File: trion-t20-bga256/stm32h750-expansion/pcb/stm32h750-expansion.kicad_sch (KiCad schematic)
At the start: 77 parts, among them J1 CONN_02x18, J2 CORTEX_DEBUG_ETM, J3 U.FL, J4 U.FL, J5 U.FL, J6 CONN_01X03, J7 CONN_01X03, J8 PMOD_HOST, M1 MECHANICAL, U1 STM32H750XBH6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

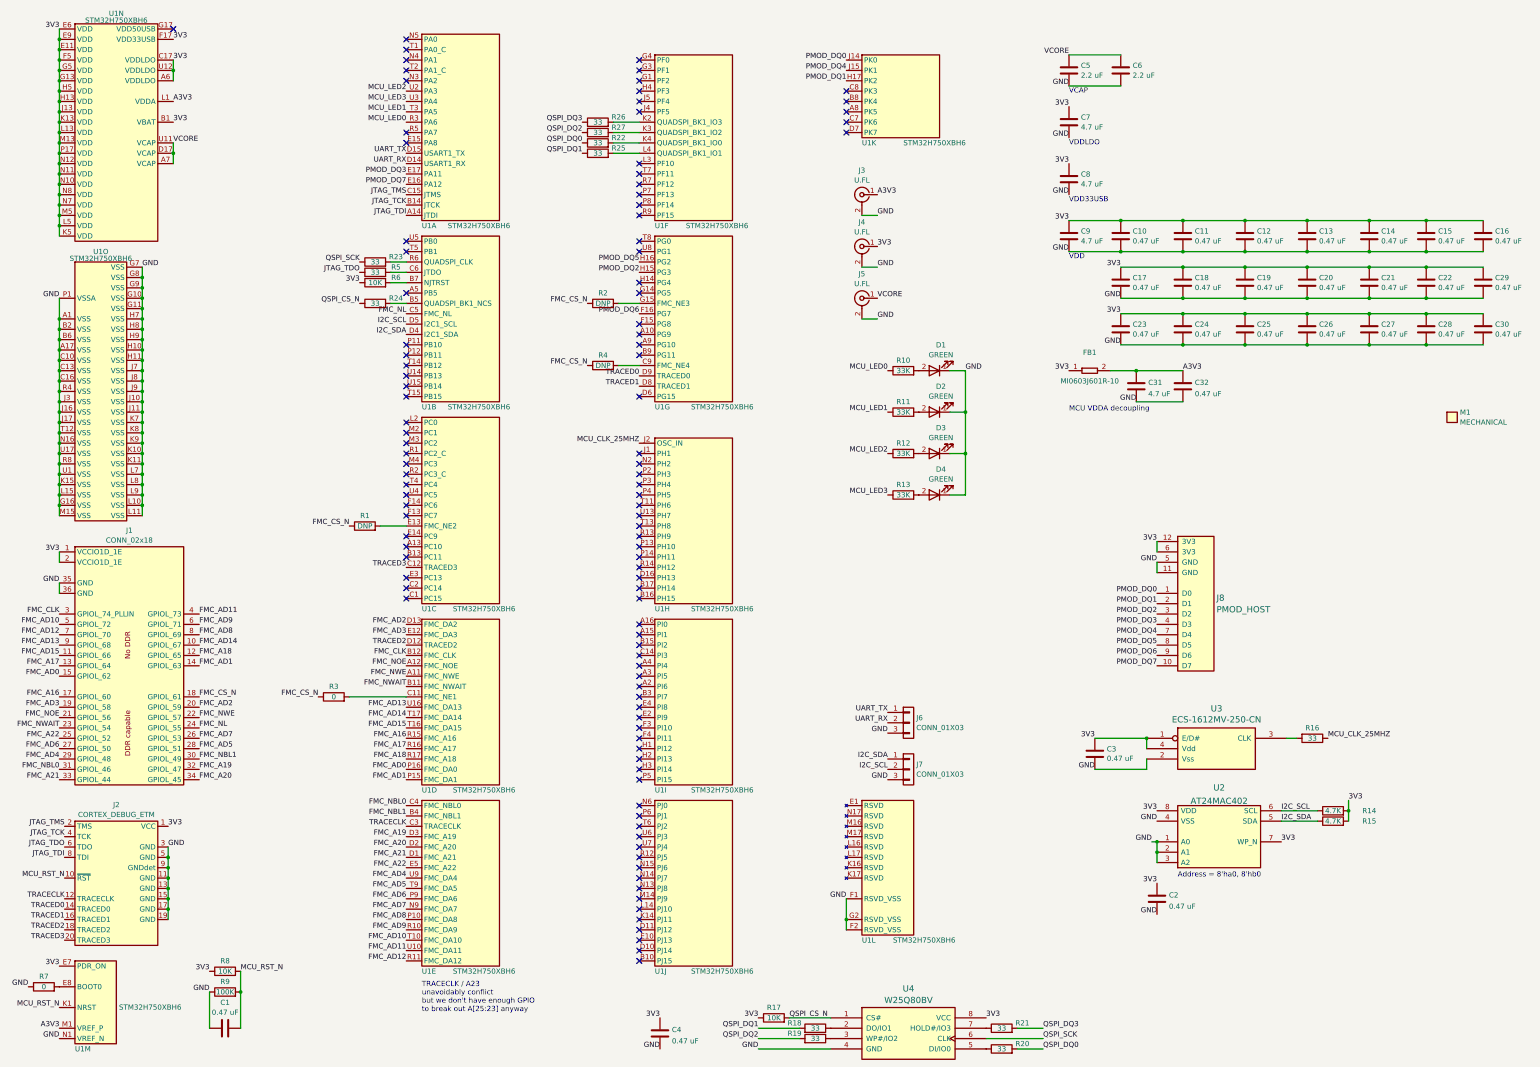
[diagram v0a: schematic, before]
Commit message: Updated stm32h750-expansion for v0.2
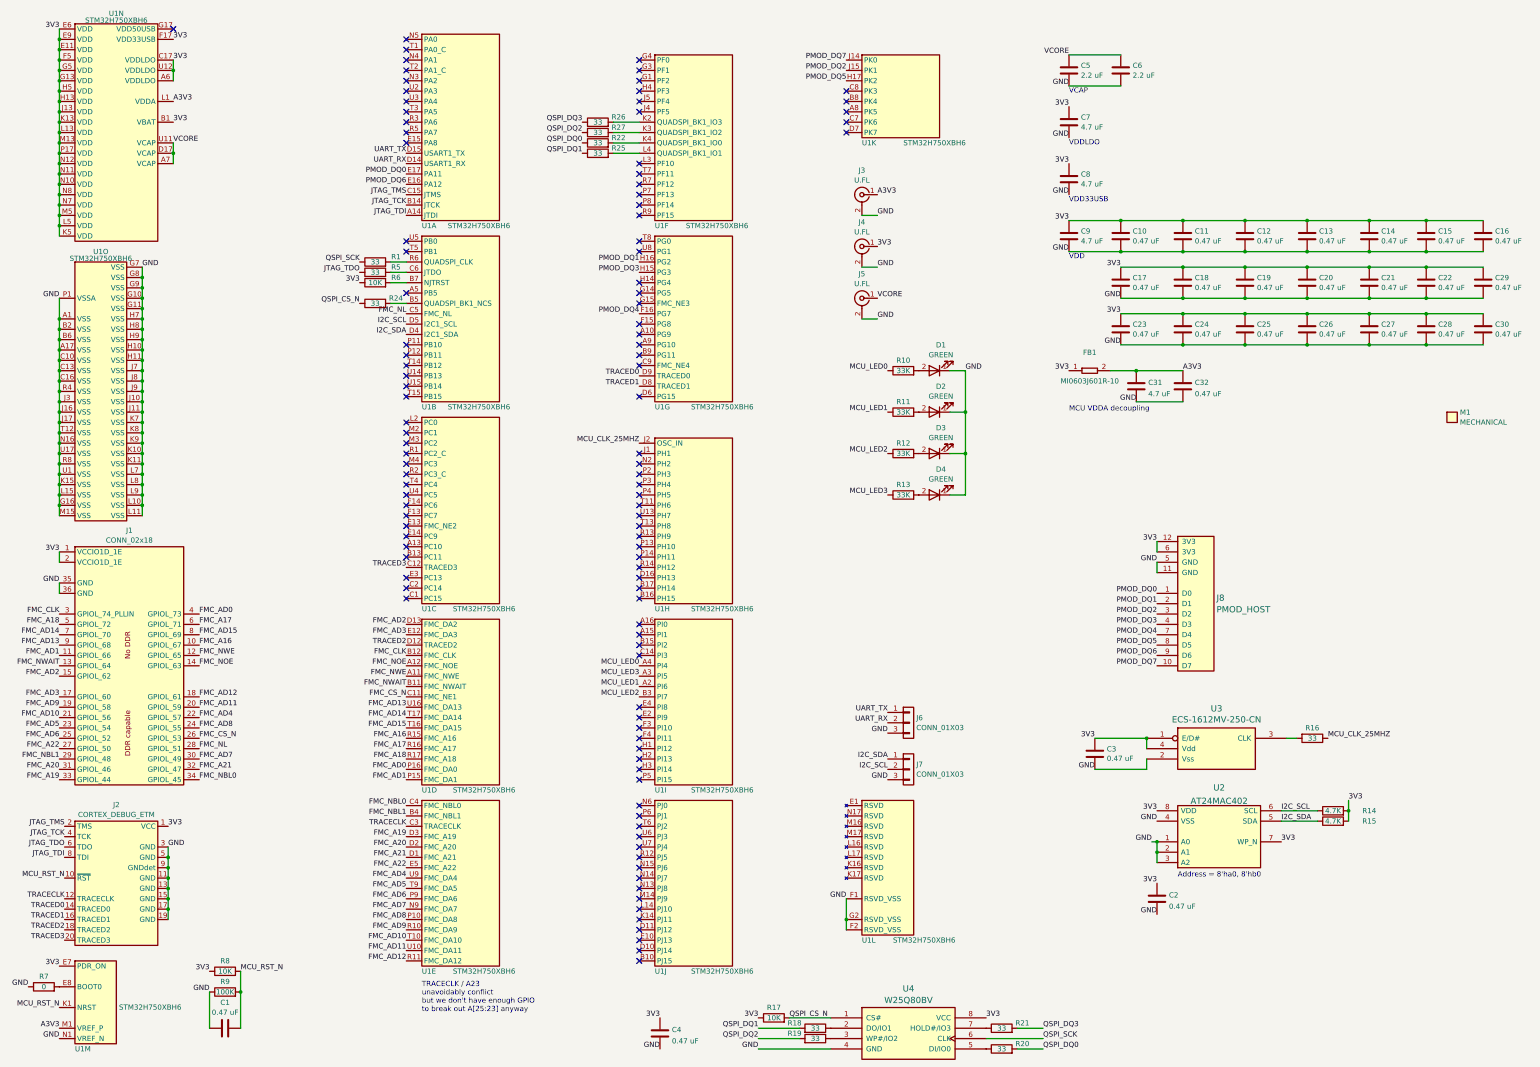
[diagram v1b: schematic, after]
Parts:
- removed R2, R4: DNP, azonenberg_pcb:EIA_0402_RES_NOSILK, symbol device:R
- removed R23: 33, azonenberg_pcb:EIA_0402_RES_NOSILK, symbol device:R
- removed R3: 0, azonenberg_pcb:EIA_0402_RES_NOSILK, symbol device:R
- R1: value DNP -> 33
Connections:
- net FMC_A16: now also J1.10 (GPIOL_67); no longer J1.17 (GPIOL_60)
- net FMC_A17: now also J1.6 (GPIOL_71); no longer J1.13 (GPIOL_64)
- net FMC_A18: now also J1.5 (GPIOL_72); no longer J1.12 (GPIOL_65)
- net FMC_A19: now also J1.33 (GPIOL_44); no longer J1.32 (GPIOL_47)
- net FMC_A20: now also J1.31 (GPIOL_46); no longer J1.34 (GPIOL_45)
- net FMC_A21: now also J1.32 (GPIOL_47); no longer J1.33 (GPIOL_44)
- net FMC_A22: now also J1.27 (GPIOL_50); no longer J1.25 (GPIOL_52)
- net FMC_AD0: now also J1.4 (GPIOL_73); no longer J1.15 (GPIOL_62)
- net FMC_AD1: now also J1.11 (GPIOL_66); no longer J1.14 (GPIOL_63)
- net FMC_AD10: now also J1.21 (GPIOL_56); no longer J1.5 (GPIOL_72)
- net FMC_AD11: now also J1.20 (GPIOL_59); no longer J1.4 (GPIOL_73)
- net FMC_AD12: now also J1.18 (GPIOL_61); no longer J1.7 (GPIOL_70)
- net FMC_AD14: now also J1.7 (GPIOL_70); no longer J1.10 (GPIOL_67)
- net FMC_AD15: now also J1.8 (GPIOL_69); no longer J1.11 (GPIOL_66)
- net FMC_AD2: now also J1.15 (GPIOL_62); no longer J1.20 (GPIOL_59)
- net FMC_AD3: now also J1.17 (GPIOL_60); no longer J1.19 (GPIOL_58)
- net FMC_AD4: now also J1.22 (GPIOL_57); no longer J1.29 (GPIOL_48)
- net FMC_AD5: now also J1.23 (GPIOL_54); no longer J1.28 (GPIOL_51)
- net FMC_AD6: now also J1.25 (GPIOL_52); no longer J1.27 (GPIOL_50)
- net FMC_AD7: now also J1.30 (GPIOL_49); no longer J1.26 (GPIOL_53)
- net FMC_AD8: now also J1.24 (GPIOL_55); no longer J1.8 (GPIOL_69)
- net FMC_AD9: now also J1.19 (GPIOL_58); no longer J1.6 (GPIOL_71)
- net FMC_CS_N: now also J1.26 (GPIOL_53), U1.C11 (PD7); no longer J1.18 (GPIOL_61), R1.1
- net FMC_NBL0: now also J1.34 (GPIOL_45); no longer J1.31 (GPIOL_46)
- net FMC_NBL1: now also J1.29 (GPIOL_48); no longer J1.30 (GPIOL_49)
- net FMC_NL: now also J1.28 (GPIOL_51); no longer J1.24 (GPIOL_55)
- net FMC_NOE: now also J1.14 (GPIOL_63); no longer J1.21 (GPIOL_56)
- net FMC_NWAIT: now also J1.13 (GPIOL_64); no longer J1.23 (GPIOL_54)
- net FMC_NWE: now also J1.12 (GPIOL_65); no longer J1.22 (GPIOL_57)
- net MCU_LED0: now also U1.A4 (PI4); no longer U1.R3 (PA6)
- net MCU_LED1: now also U1.A2 (PI6); no longer U1.T3 (PA5)
- net MCU_LED2: now also U1.B3 (PI7); no longer U1.U2 (PA3)
- net MCU_LED3: now also U1.A3 (PI5); no longer U1.U3 (PA4)
- net PMOD_DQ0: now also U1.E17 (PA11); no longer U1.J14 (PK0)
- net PMOD_DQ1: now also U1.H16 (PG2); no longer U1.H17 (PK2)
- net PMOD_DQ2: now also U1.J15 (PK1); no longer U1.H15 (PG3)
- net PMOD_DQ3: now also U1.H15 (PG3); no longer U1.E17 (PA11)
- net PMOD_DQ4: now also U1.F16 (PG7); no longer U1.J15 (PK1)
- net PMOD_DQ5: now also U1.H17 (PK2); no longer U1.H16 (PG2)
- net PMOD_DQ6: now also U1.E16 (PA12); no longer U1.F16 (PG7)
- net PMOD_DQ7: now also U1.J14 (PK0); no longer U1.E16 (PA12)
- net QSPI_SCK: now also R1.1
- net at U1.R6 (PB2): now also R1.2
- net at U1.E13 (PC8): no longer R1.2
- no-connect marks 106 -> 109
